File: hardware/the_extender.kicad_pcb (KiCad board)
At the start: 4 copper layers, 51.2 x 51.2 mm, 120 parts, among them J0 TYPE-C 24P QT 143, J1 TYPE-C-31-M-16, J2 U231-091N-3BLRC11, J3 PJ-327D-5A, J4 PJ-327D-5A, J5 AF 10.0 HC6.3, Q1 SSM3J332R,LF, Q2 SSM3J332R,LF, Q3 SSM3J332R,LF, Q4 PMBT3904,215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

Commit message: silkscreen schubsen
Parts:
- moved R29 0.05 mm to (59.8, 38.6)
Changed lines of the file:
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@@
     (attr smd)
     (fp_text reference "C12" (at -0.0375 -0.1) (layer "F.SilkS")
-        (effects (font (size 1 1) (thickness 0.15)))
+        (effects (font (size 1 0.5) (thickness 0.125)))
     )
     (fp_text value "22u" (at 0 1.85) (layer "F.Fab")
@@
     (attr smd)
     (fp_text reference "C1" (at -0.0375 0) (layer "F.SilkS")
-        (effects (font (size 1 1) (thickness 0.15)))
+        (effects (font (size 1 0.5) (thickness 0.125)))
     )
     (fp_text value "22u" (at 0 1.85) (layer "F.Fab")
@@
     (attr smd)
     (fp_text reference "C7" (at -0.0375 0) (layer "F.SilkS")
-        (effects (font (size 1 1) (thickness 0.15)))
+        (effects (font (size 1 0.5) (thickness 0.125)))
     )
     (fp_text value "22u" (at 0 1.85) (layer "F.Fab")
@@
     (property "ki_keywords" "cap capacitor")
     (attr smd)
-    (fp_text reference "C47" (at -0.0375 0 90) (layer "F.SilkS")
+    (fp_text reference "C47" (at -3.9375 -5.4 90) (layer "F.SilkS")
         (effects (font (size 1 1) (thickness 0.15)))
     )
@@
     (property "ki_keywords" "R res resistor")
     (attr smd)
-    (fp_text reference "R2" (at 0 -1.65 90) (layer "F.SilkS")
-        (effects (font (size 1 1) (thickness 0.15)))
+    (fp_text reference "R2" (at 0 1.2 90) (layer "F.SilkS")
+        (effects (font (size 0.5 1) (thickness 0.125)))
     )
     (fp_text value "10k" (at 0 1.65 90) (layer "F.Fab")
@@
     (property "ki_keywords" "R res resistor")
     (attr smd)
-    (fp_text reference "R5" (at -2.8 -0.3) (layer "F.SilkS")
+    (fp_text reference "R5" (at -2.4 0 90) (layer "F.SilkS")
         (effects (font (size 1 1) (thickness 0.15)))
     )
@@
     (property "ki_keywords" "R res resistor")
     (attr smd)
-    (fp_text reference "R10" (at 0 0.1 180) (layer "F.SilkS")
-        (effects (font (size 1 1) (thickness 0.15)))
+    (fp_text reference "R10" (at 0 1.2 180) (layer "F.SilkS")
+        (effects (font (size 0.5 0.75) (thickness 0.125)))
     )
     (fp_text value "1k" (at 0 1.65) (layer "F.Fab")
@@
     (property "ki_keywords" "R res resistor")
     (attr smd)
-    (fp_text reference "R11" (at -0.111 -7.77) (layer "F.SilkS")
+    (fp_text reference "R11" (at -0.011 -9.07) (layer "F.SilkS")
         (effects (font (size 1 1) (thickness 0.15)))
     )
@@
     (property "ki_keywords" "R res resistor")
     (attr smd)
-    (fp_text reference "R3" (at 0.1 0 90) (layer "F.SilkS")
+    (fp_text reference "R3" (at -0.2 10.5 180) (layer "F.SilkS")
         (effects (font (size 1 1) (thickness 0.15)))
     )
@@
     (property "ki_keywords" "cap capacitor")
     (attr smd)
-    (fp_text reference "C8" (at -0.0625 0 270) (layer "F.SilkS")
-        (effects (font (size 1 1) (thickness 0.15)))
+    (fp_text reference "C8" (at -0.0625 0) (layer "F.SilkS")
+        (effects (font (size 1 0.5) (thickness 0.125)))
     )
     (fp_text value "22u" (at 0 1.85) (layer "F.Fab")
@@
     (property "ki_keywords" "R res resistor")
     (attr smd)
-    (fp_text reference "R4" (at 0 6) (layer "F.SilkS")
+    (fp_text reference "R4" (at 0 7.3) (layer "F.SilkS")
         (effects (font (size 1 1) (thickness 0.15)))
     )
@@
   )
   (footprint "Resistor_SMD:R_0805_2012Metric_Pad1.20x1.40mm_HandSolder" (layer "F.Cu")
-    (at 59.8 38.6 -90)
+    (at 59.81 38.65 -90)
     (descr "Resistor SMD 0805 (2012 Metric), square (rectangular) end terminal, IPC_7351 nominal with elongated pad for handsoldering. (Body size source: IPC-SM-782 page 72, https://www.pcb-3d.com/wordpress/wp-content/uploads/ipc-sm-782a_amendment_1_and_2.pdf), generated with kicad-footprint-generator")
     (tags "resistor handsolder")
@@
     (property "ki_keywords" "R res resistor")
     (attr smd)
-    (fp_text reference "R29" (at 0.1 -0.1 90) (layer "F.SilkS")
+    (fp_text reference "R29" (at 4 4.8 -90) (layer "F.SilkS")
         (effects (font (size 1 1) (thickness 0.15)))
     )
@@
     (property "ki_keywords" "cap capacitor")
     (attr smd)
-    (fp_text reference "C29" (at 3.087 0 90) (layer "F.SilkS")
+    (fp_text reference "C29" (at -3.113 -0.178 90) (layer "F.SilkS")
         (effects (font (size 1 1) (thickness 0.15)))
     )
@@
     (property "ki_keywords" "R res resistor")
     (attr smd)
-    (fp_text reference "R7" (at 0 0 180) (layer "F.SilkS")
-        (effects (font (size 1 1) (thickness 0.15)))
+    (fp_text reference "R7" (at 0 1.3 180) (layer "F.SilkS")
+        (effects (font (size 0.5 0.75) (thickness 0.125)))
     )
     (fp_text value "2k2" (at 0 1.65) (layer "F.Fab")
@@
     (property "ki_keywords" "transistor PMOS P-MOS P-MOSFET")
     (attr smd)
-    (fp_text reference "Q2" (at 0 -2.5) (layer "F.SilkS")
+    (fp_text reference "Q2" (at 1.8 1.15) (layer "F.SilkS")
         (effects (font (size 1 1) (thickness 0.15)))
     )
@@
     (property "ki_keywords" "LED RGB diode")
     (attr smd)
-    (fp_text reference "D1" (at 2.238 0.1526 -180) (layer "F.SilkS")
-        (effects (font (size 1 1) (thickness 0.15)))
+    (fp_text reference "D1" (at 2.038 0.5526) (layer "F.SilkS")
+        (effects (font (size 0.5 1) (thickness 0.125)))
     )
     (fp_text value "MHSC110RGBCT" (at 0 4.15 90) (layer "F.Fab") hide
@@
     (property "ki_keywords" "cap capacitor")
     (attr smd)
-    (fp_text reference "C30" (at -3.1695 0.01 90) (layer "F.SilkS")
+    (fp_text reference "C30" (at -3.1695 -0.39 90) (layer "F.SilkS")
         (effects (font (size 1 1) (thickness 0.15)))
     )
@@
     (property "ki_keywords" "R res resistor")
     (attr smd)
-    (fp_text reference "R20" (at -3.087 0 90) (layer "F.SilkS")
+    (fp_text reference "R20" (at 3.113 -0.454 90) (layer "F.SilkS")
         (effects (font (size 1 1) (thickness 0.15)))
     )
@@
     (property "ki_keywords" "diode")
     (attr smd)
-    (fp_text reference "D2" (at -0.087 -8.532 180) (layer "F.SilkS")
+    (fp_text reference "D2" (at 0.013 -9.832 180) (layer "F.SilkS")
         (effects (font (size 1 1) (thickness 0.15)))
     )
@@
     (property "ki_keywords" "R res resistor")
     (attr smd)
-    (fp_text reference "R12" (at -0.016 7.135) (layer "F.SilkS")
+    (fp_text reference "R12" (at -0.116 8.435) (layer "F.SilkS")
         (effects (font (size 1 1) (thickness 0.15)))
     )
@@
     (property "ki_keywords" "cap capacitor")
     (attr smd)
-    (fp_text reference "C6" (at 0.0375 0 90) (layer "F.SilkS")
+    (fp_text reference "C6" (at -3.2625 -0.1 90) (layer "F.SilkS")
         (effects (font (size 1 1) (thickness 0.15)))
     )
@@
       (net 50 "Net-(U2-QSPI_SS)") (pinfunction "1") (pintype "passive"))
   )
-  (gr_rect (start 63.5 43.7) (end 66.8 49.2)
+  (gr_rect (start 63.4 43.7) (end 66.7 50.4)
     (stroke (width 0.15) (type default)) (fill none) (layer "F.SilkS"))
+  (gr_line (start 60.545 38.65) (end 61.065 38.6625)
+    (stroke (width 0.15) (type default)) (layer "F.SilkS"))
   (gr_rect (start 80.3 62.8) (end 83.8 68.8)
     (stroke (width 0.15) (type default)) (fill none) (layer "F.SilkS"))
+  (gr_line (start 60.8 40.4) (end 60.805 38.65125)
+    (stroke (width 0.15) (type default)) (layer "F.SilkS"))
+  (gr_line (start 57.2 41) (end 58.6 41)
+    (stroke (width 0.15) (type default)) (layer "F.SilkS"))
   (gr_line (start 48.26 54.61) (end 47.752 54.229)
     (stroke (width 0.15) (type solid)) (layer "F.SilkS"))
+  (gr_line (start 58.6 41) (end 59 40.4)
+    (stroke (width 0.15) (type default)) (layer "F.SilkS"))
+  (gr_rect (start 54.2 41) (end 57.2 44.2)
+    (stroke (width 0.15) (type default)) (fill none) (layer "F.SilkS"))
   (gr_rect (start 58.4 46) (end 62 50.3)
     (stroke (width 0.15) (type default)) (fill none) (layer "F.SilkS"))
@@
   (gr_line (start 83.8 62.8) (end 87.4 59)
     (stroke (width 0.15) (type default)) (layer "F.SilkS"))
+  (gr_line (start 59 40.4) (end 60.8 40.4)
+    (stroke (width 0.15) (type default)) (layer "F.SilkS"))
   (gr_rect (start 91.948 69.596) (end 96.52 73.406)
     (stroke (width 0) (type solid)) (fill solid) (layer "B.Mask"))
@@
   (gr_circle (center 71.26 33.875) (end 71.66 33.875)
     (stroke (width 0) (type solid)) (fill solid) (layer "B.Mask"))
-  (gr_circle (center 95.89 48.64) (end 96.29 48.64)
-    (stroke (width 0) (type solid)) (fill solid) (layer "B.Mask"))
   (gr_circle (center 90.45 59.62) (end 90.85 59.62)
     (stroke (width 0) (type solid)) (fill solid) (layer "B.Mask"))
@@
   (via (at 64.77 51.054) (size 0.8) (drill 0.4) (layers "F.Cu" "B.Cu") (free) (net 2))
   (via (at 75.438 56.769) (size 0.8) (drill 0.4) (layers "F.Cu" "B.Cu") (free) (net 2))
-  (via (at 95.885 48.641) (size 0.8) (drill 0.4) (layers "F.Cu" "B.Cu") (net 2))
+  (via (at 96 49.2) (size 0.8) (drill 0.4) (layers "F.Cu" "B.Cu") (net 2))
   (via (at 69.723 40.132) (size 0.8) (drill 0.4) (layers "F.Cu" "B.Cu") (free) (net 2))
   (via (at 80.645 65.913) (size 0.8) (drill 0.4) (layers "F.Cu" "B.Cu") (free) (net 2))

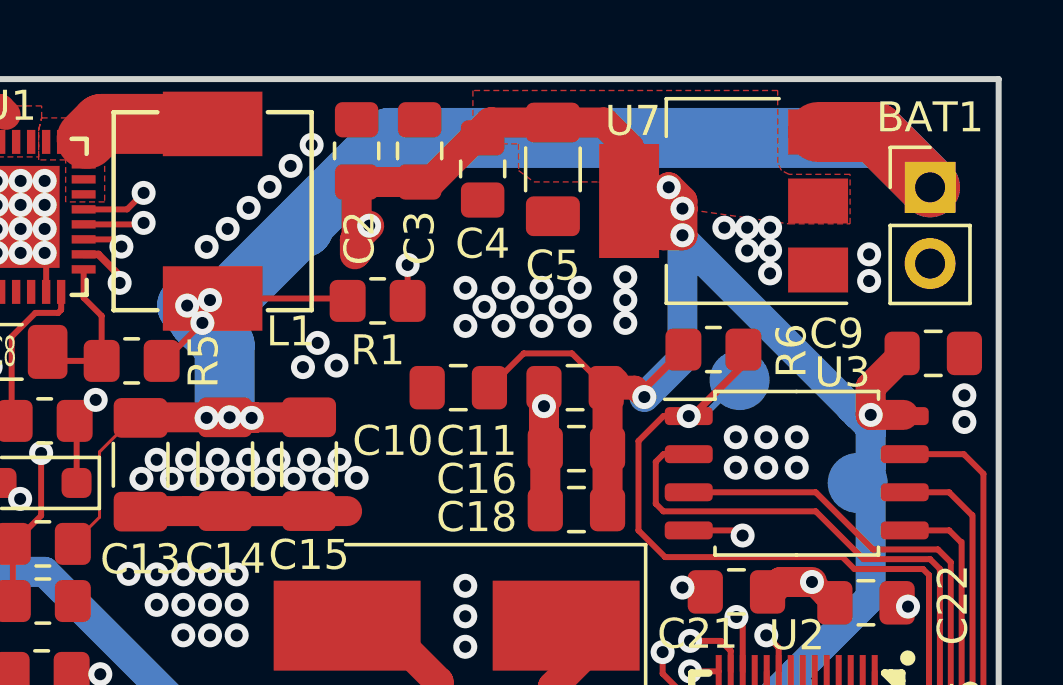
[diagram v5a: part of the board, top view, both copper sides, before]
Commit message: add Li-Ion protection circuit
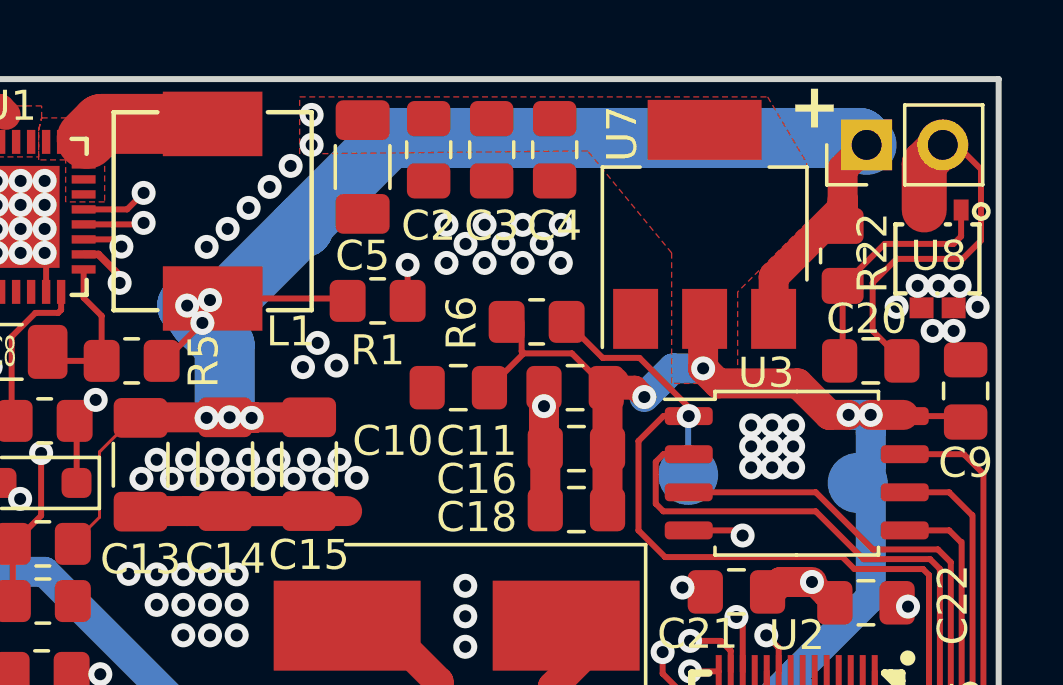
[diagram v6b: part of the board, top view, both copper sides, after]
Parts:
- added C20: 100n, Capacitor_SMD:C_0805_2012Metric_Pad1.18x1.45mm_HandSolder, F.Cu at (92.6, 32.0)
- added R22: 1k, Resistor_SMD:R_0805_2012Metric_Pad1.20x1.40mm_HandSolder, F.Cu at (91.7, 28.5)
- added U8: XB4908A, easyeda2kicad:ESN-4_L2.8-W2.3-LS3.7-BL, F.Cu at (95.0, 28.6)
- moved C5 6.34 mm to (75.7, 25.5)
- moved R6 5.96 mm to (81.5, 30.7)
- moved TP1 3.60 mm to (86.5, 35.8)
- moved BAT1 2.54 mm to (92.5, 24.8), turned to 90 degrees
- moved C4 2.48 mm to (82.1, 25.0)
- moved C2 2.40 mm to (77.9, 25.0), turned to -90 degrees
- moved C3 2.40 mm to (80.0, 25.0), turned to -90 degrees
- moved C9 1.65 mm to (95.8, 33.0), turned to 90 degrees
- moved U7 1.00 mm to (87.1, 27.4), turned to 90 degrees
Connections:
- BAT1 pad 2: GND -> -BATT
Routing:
- net +3V3: track 194.7 -> 146.0 mm, vias 14 -> 13
- net -BATT: track 0.00 -> 13.6 mm
- net Net-(U8-VDD): track 0.00 -> 8.05 mm
- net Net-(U2-QSPI_SS): track 24.3 -> 27.3 mm
- net +BATT: track 57.6 -> 58.4 mm
- net GND: vias 351 -> 348
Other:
- board text added: "+"

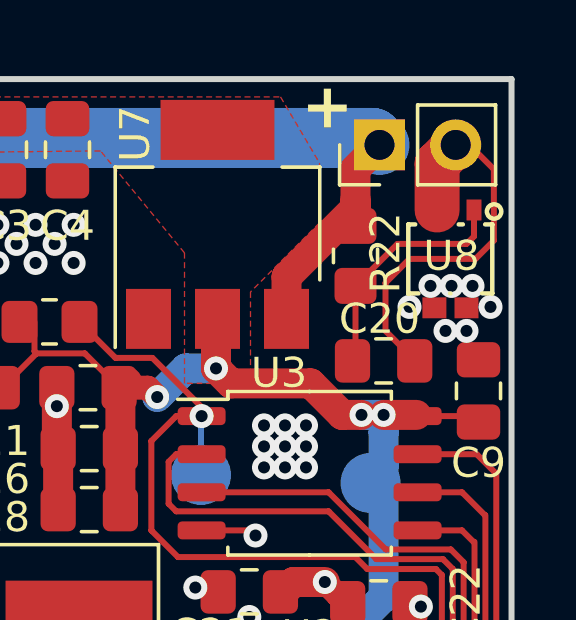
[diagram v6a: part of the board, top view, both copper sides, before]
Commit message: cell protection fixes
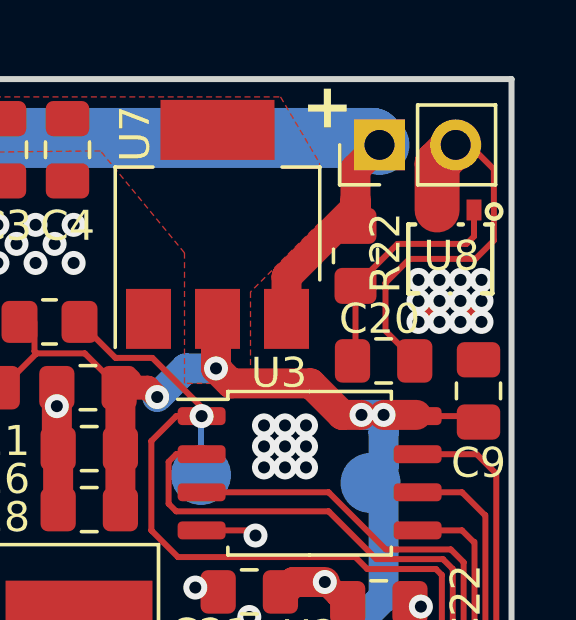
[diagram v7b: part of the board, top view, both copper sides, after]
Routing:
- net GND: vias 348 -> 353
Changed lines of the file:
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@@
   (gr_circle (center 69.35 53.43) (end 69.75 53.43)
     (stroke (width 0) (type solid)) (fill solid) (layer "B.Mask"))
+  (gr_rect (start 93.4 28.9) (end 96.3 31.1)
+    (stroke (width 0.15) (type solid)) (fill solid) (layer "B.Mask"))
   (gr_circle (center 72 33.9) (end 72.4 33.9)
     (stroke (width 0) (type solid)) (fill solid) (layer "B.Mask"))
@@
   (via (at 74.549 45.212) (size 0.8) (drill 0.4) (layers "F.Cu" "B.Cu") (free) (net 2))
   (via (at 65.405 44.958) (size 0.8) (drill 0.4) (layers "F.Cu" "B.Cu") (net 2))
+  (via (at 93.8 29.3) (size 0.8) (drill 0.4) (layers "F.Cu" "B.Cu") (free) (net 2))
   (via (at 88.65 34.85) (size 0.8) (drill 0.4) (layers "F.Cu" "B.Cu") (free) (net 2))
   (via (at 68.326 51.816) (size 0.8) (drill 0.4) (layers "F.Cu" "B.Cu") (free) (net 2))
   (via (at 79.375 64.6176) (size 0.8) (drill 0.4) (layers "F.Cu" "B.Cu") (free) (net 2))
-  (via (at 96.2 30.2) (size 0.8) (drill 0.4) (layers "F.Cu" "B.Cu") (free) (net 2))
   (via (at 87.249 64.008) (size 0.8) (drill 0.4) (layers "F.Cu" "B.Cu") (free) (net 2))
   (via (at 55.4 28.6) (size 0.8) (drill 0.4) (layers "F.Cu" "B.Cu") (net 2))
@@
   (via (at 89.154 46.863) (size 0.8) (drill 0.4) (layers "F.Cu" "B.Cu") (net 2))
   (via (at 90.4455 60.3504) (size 0.8) (drill 0.4) (layers "F.Cu" "B.Cu") (net 2))
+  (via (at 95.2 30) (size 0.8) (drill 0.4) (layers "F.Cu" "B.Cu") (net 2))
   (via (at 83.566 71.882) (size 0.8) (drill 0.4) (layers "F.Cu" "B.Cu") (free) (net 2))
   (via (at 87.092812 53.3005) (size 0.8) (drill 0.4) (layers "F.Cu" "B.Cu") (free) (net 2))
@@
   (via (at 64.389 47.117) (size 0.8) (drill 0.4) (layers "F.Cu" "B.Cu") (net 2))
   (via (at 63.373 48.133) (size 0.8) (drill 0.4) (layers "F.Cu" "B.Cu") (net 2))
-  (via (at 94.2 29.5) (size 0.8) (drill 0.4) (layers "F.Cu" "B.Cu") (free) (net 2))
+  (via (at 95.9 30.7) (size 0.8) (drill 0.4) (layers "F.Cu" "B.Cu") (free) (net 2))
   (via (at 74.549 46.101) (size 0.8) (drill 0.4) (layers "F.Cu" "B.Cu") (net 2))
   (via (at 47.244 27.94) (size 0.8) (drill 0.4) (layers "F.Cu" "B.Cu") (free) (net 2))
@@
   (via (at 89.027 62.484) (size 0.8) (drill 0.4) (layers "F.Cu" "B.Cu") (free) (net 2))
   (via (at 62.357 46.101) (size 0.8) (drill 0.4) (layers "F.Cu" "B.Cu") (net 2))
-  (via (at 95.6 29.5) (size 0.8) (drill 0.4) (layers "F.Cu" "B.Cu") (free) (net 2))
   (via (at 85.3 61.2) (size 0.8) (drill 0.4) (layers "F.Cu" "B.Cu") (free) (net 2))
   (via (at 91.186 44.958) (size 0.8) (drill 0.4) (layers "F.Cu" "B.Cu") (net 2))
@@
   (via (at 81.026 71.882) (size 0.8) (drill 0.4) (layers "F.Cu" "B.Cu") (free) (net 2))
   (via (at 83.185 64.643) (size 0.8) (drill 0.4) (layers "F.Cu" "B.Cu") (free) (net 2))
-  (via (at 94.9 29.5) (size 0.8) (drill 0.4) (layers "F.Cu" "B.Cu") (free) (net 2))
   (via (at 67.437 48.133) (size 0.8) (drill 0.4) (layers "F.Cu" "B.Cu") (net 2))
   (via (at 47.879 44.069) (size 0.8) (drill 0.4) (layers "F.Cu" "B.Cu") (free) (net 2))
@@
   (via (at 88.011 64.008) (size 0.8) (drill 0.4) (layers "F.Cu" "B.Cu") (free) (net 2))
   (via (at 69.723 41.148) (size 0.8) (drill 0.4) (layers "F.Cu" "B.Cu") (free) (net 2))
+  (via (at 94.5 29.3) (size 0.8) (drill 0.4) (layers "F.Cu" "B.Cu") (free) (net 2))
   (via (at 74.676 55.245) (size 0.8) (drill 0.4) (layers "F.Cu" "B.Cu") (free) (net 2))
   (via (at 90.551 61.087) (size 0.8) (drill 0.4) (layers "F.Cu" "B.Cu") (free) (net 2))
@@
   (via (at 64.77 51.816) (size 0.8) (drill 0.4) (layers "F.Cu" "B.Cu") (free) (net 2))
   (via (at 66.421 43.815) (size 0.8) (drill 0.4) (layers "F.Cu" "B.Cu") (net 2))
+  (via (at 93.8 30) (size 0.8) (drill 0.4) (layers "F.Cu" "B.Cu") (free) (net 2))
   (via (at 58.674 72.136) (size 0.8) (drill 0.4) (layers "F.Cu" "B.Cu") (free) (net 2))
   (via (at 47.244 30.226) (size 0.8) (drill 0.4) (layers "F.Cu" "B.Cu") (free) (net 2))
@@
   (via (at 65.405 46.101) (size 0.8) (drill 0.4) (layers "F.Cu" "B.Cu") (net 2))
   (via (at 83.058 56.769) (size 0.8) (drill 0.4) (layers "F.Cu" "B.Cu") (net 2))
-  (via (at 94.7 31) (size 0.8) (drill 0.4) (layers "F.Cu" "B.Cu") (free) (net 2))
   (via (at 62.357 48.133) (size 0.8) (drill 0.4) (layers "F.Cu" "B.Cu") (net 2))
   (via (at 47.244 25.654) (size 0.8) (drill 0.4) (layers "F.Cu" "B.Cu") (free) (net 2))
@@
   (via (at 47.244 26.416) (size 0.8) (drill 0.4) (layers "F.Cu" "B.Cu") (free) (net 2))
   (via (at 55.9 27.2) (size 0.8) (drill 0.4) (layers "F.Cu" "B.Cu") (net 2))
+  (via (at 95.2 29.3) (size 0.8) (drill 0.4) (layers "F.Cu" "B.Cu") (free) (net 2))
   (via (at 51.943 58.42) (size 0.8) (drill 0.4) (layers "F.Cu" "B.Cu") (free) (net 2))
   (via (at 82.296 72.898) (size 0.8) (drill 0.4) (layers "F.Cu" "B.Cu") (free) (net 2))
@@
   (via (at 81.922 61.1) (size 0.8) (drill 0.4) (layers "F.Cu" "B.Cu") (free) (net 2))
   (via (at 64.389 43.815) (size 0.8) (drill 0.4) (layers "F.Cu" "B.Cu") (net 2))
-  (via (at 93.5 30.2) (size 0.8) (drill 0.4) (layers "F.Cu" "B.Cu") (free) (net 2))
   (via (at 68.834 62.23) (size 0.8) (drill 0.4) (layers "F.Cu" "B.Cu") (free) (net 2))
   (via (at 63.373 43.815) (size 0.8) (drill 0.4) (layers "F.Cu" "B.Cu") (net 2))
@@
   (via (at 73.914 52.578) (size 0.8) (drill 0.4) (layers "F.Cu" "B.Cu") (net 2))
   (via (at 72.39 35.932) (size 0.8) (drill 0.4) (layers "F.Cu" "B.Cu") (free) (net 2))
+  (via (at 95.9 30) (size 0.8) (drill 0.4) (layers "F.Cu" "B.Cu") (free) (net 2))
   (via (at 63.5 27.6) (size 0.8) (drill 0.4) (layers "F.Cu" "B.Cu") (net 2))
   (via (at 68.759011 64.4535) (size 0.8) (drill 0.4) (layers "F.Cu" "B.Cu") (free) (net 2))
+  (via (at 94.5 30.7) (size 0.8) (drill 0.4) (layers "F.Cu" "B.Cu") (free) (net 2))
   (via (at 82.811 61.1) (size 0.8) (drill 0.4) (layers "F.Cu" "B.Cu") (free) (net 2))
-  (via (at 95.4 31) (size 0.8) (drill 0.4) (layers "F.Cu" "B.Cu") (free) (net 2))
   (via (at 82.305 27.465) (size 0.8) (drill 0.4) (layers "F.Cu" "B.Cu") (free) (net 2))
   (via (at 48.006 29.464) (size 0.8) (drill 0.4) (layers "F.Cu" "B.Cu") (free) (net 2))
@@
   (via (at 47.879 46.355) (size 0.8) (drill 0.4) (layers "F.Cu" "B.Cu") (free) (net 2))
   (via (at 73.914 54.864) (size 0.8) (drill 0.4) (layers "F.Cu" "B.Cu") (free) (net 2))
+  (via (at 95.2 30.7) (size 0.8) (drill 0.4) (layers "F.Cu" "B.Cu") (free) (net 2))
+  (via (at 95.9 29.3) (size 0.8) (drill 0.4) (layers "F.Cu" "B.Cu") (free) (net 2))
   (via (at 47.625 40.005) (size 0.8) (drill 0.4) (layers "F.Cu" "B.Cu") (free) (net 2))
+  (via (at 93.8 30.7) (size 0.8) (drill 0.4) (layers "F.Cu" "B.Cu") (free) (net 2))
   (via (at 63.5 28.4) (size 0.8) (drill 0.4) (layers "F.Cu" "B.Cu") (net 2))
   (via (at 75.438 58.293) (size 0.8) (drill 0.4) (layers "F.Cu" "B.Cu") (free) (net 2))
@@
   (via (at 79.765 27.465) (size 0.8) (drill 0.4) (layers "F.Cu" "B.Cu") (free) (net 2))
   (via (at 68.453 47.117) (size 0.8) (drill 0.4) (layers "F.Cu" "B.Cu") (net 2))
+  (via (at 94.5 30) (size 0.8) (drill 0.4) (layers "F.Cu" "B.Cu") (net 2))
   (via (at 59.3 31.2) (size 0.8) (drill 0.4) (layers "F.Cu" "B.Cu") (net 2))
   (via (at 88.65 34.15) (size 0.8) (drill 0.4) (layers "F.Cu" "B.Cu") (free) (net 2))
